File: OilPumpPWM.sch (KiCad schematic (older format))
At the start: 3 parts, among them Q1 MMBT3904

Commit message: Checkpoint before trying 4 layer
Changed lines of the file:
@@
 $Descr A4 11693 8268
 encoding utf-8
-Sheet 26 50
+Sheet 36 37
 Title ""
 Date ""
@@
 AR Path="/60483BB8/6056205F/60583721" Ref="Q4"  Part="1"
 AR Path="/614844F4/60583721" Ref="Q1"  Part="1"
-F 0 "Q4" H 5591 3846 50  0000 L CNN
+AR Path="/622024A9/60583721" Ref="Q4"  Part="1"
+AR Path="/622119D7/60583721" Ref="Q7"  Part="1"
+F 0 "Q7" H 5591 3846 50  0000 L CNN
 F 1 "MMBT3904" H 5591 3755 50  0000 L CNN
 F 2 "Package_TO_SOT_SMD:SOT-23" H 5600 3725 50  0001 L CIN
@@
 AR Path="/60483BB8/6056205F/60583722" Ref="R1"  Part="1"
 AR Path="/614844F4/60583722" Ref="R35"  Part="1"
-F 0 "R1" V 4195 3800 50  0000 C CNN
+AR Path="/622024A9/60583722" Ref="R1"  Part="1"
+AR Path="/622119D7/60583722" Ref="R4"  Part="1"
+F 0 "R4" V 4195 3800 50  0000 C CNN
 F 1 "1K" V 4286 3800 50  0000 C CNN
 F 2 "Resistor_SMD:R_0805_2012Metric" V 4440 3790 50  0001 C CNN
@@
 AR Path="/60483BB8/6056205F/60583723" Ref="R2"  Part="1"
 AR Path="/614844F4/60583723" Ref="R36"  Part="1"
-F 0 "R2" H 7268 3246 50  0000 L CNN
+AR Path="/622024A9/60583723" Ref="R2"  Part="1"
+AR Path="/622119D7/60583723" Ref="R11"  Part="1"
+F 0 "R11" H 7268 3246 50  0000 L CNN
 F 1 "1K" H 7268 3155 50  0000 L CNN
 F 2 "Resistor_SMD:R_0805_2012Metric" V 7240 3190 50  0001 C CNN

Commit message: Routed PCB
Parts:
- Q1: JLCPCB_PN (none) -> C20526
- R35, R36: JLCPCB_PN (none) -> C17513
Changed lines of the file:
@@
 F 2 "Package_TO_SOT_SMD:SOT-23" H 5600 3725 50  0001 L CIN
 F 3 "https://www.fairchildsemi.com/datasheets/2N/2N3904.pdf" H 5400 3800 50  0001 L CNN
+F 4 "C20526" H 5400 3800 50  0001 C CNN "JLCPCB_PN"
 	1    5400 3800
 	1    0    0    -1
@@
 F 2 "Resistor_SMD:R_0805_2012Metric" V 4440 3790 50  0001 C CNN
 F 3 "~" H 4400 3800 50  0001 C CNN
+F 4 "C17513" H 4400 3800 50  0001 C CNN "JLCPCB_PN"
 	1    4400 3800
 	0    1    1    0
@@
 F 2 "Resistor_SMD:R_0805_2012Metric" V 7240 3190 50  0001 C CNN
 F 3 "~" H 7200 3200 50  0001 C CNN
+F 4 "C17513" H 7200 3200 50  0001 C CNN "JLCPCB_PN"
 	1    7200 3200
 	1    0    0    -1

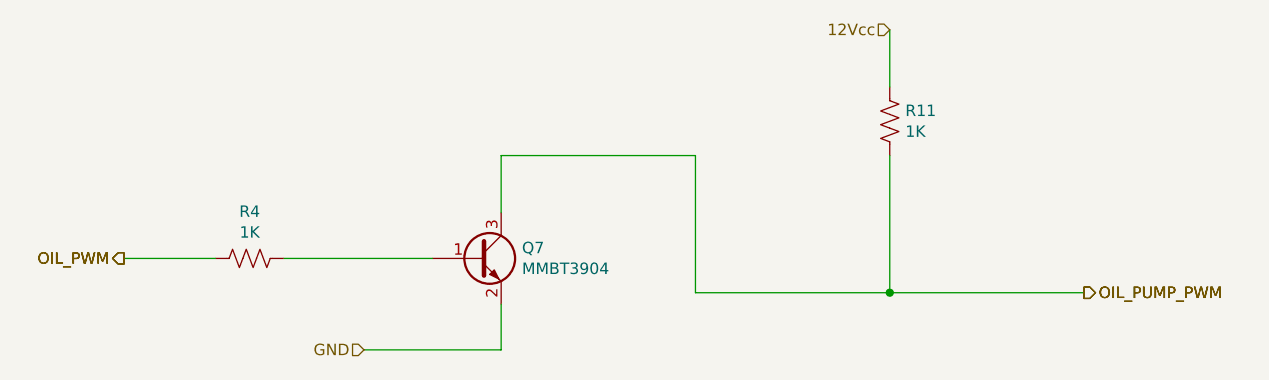
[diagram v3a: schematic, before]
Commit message: Checkpoint 2022-01-19
Design with bluepill to run the heater since we lose some of the SPI
pins to the USB port on the STM32-H107.
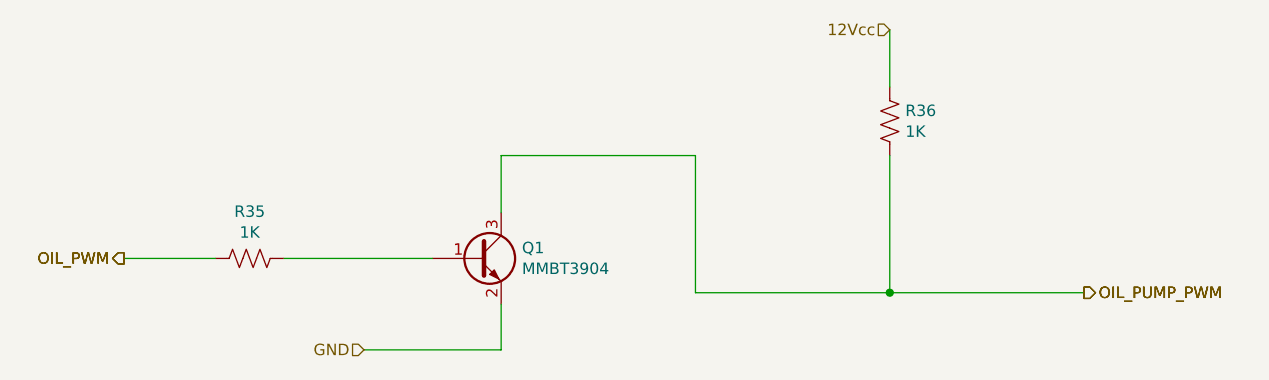
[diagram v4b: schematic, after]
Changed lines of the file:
@@
 $Descr A4 11693 8268
 encoding utf-8
-Sheet 30 36
+Sheet 29 37
 Title ""
 Date ""
@@
 AR Path="/622024A9/60583721" Ref="Q4"  Part="1"
 AR Path="/622119D7/60583721" Ref="Q7"  Part="1"
-F 0 "Q7" H 5591 3846 50  0000 L CNN
+F 0 "Q1" H 5591 3846 50  0000 L CNN
 F 1 "MMBT3904" H 5591 3755 50  0000 L CNN
 F 2 "Package_TO_SOT_SMD:SOT-23" H 5600 3725 50  0001 L CIN
@@
 AR Path="/622024A9/60583722" Ref="R1"  Part="1"
 AR Path="/622119D7/60583722" Ref="R4"  Part="1"
-F 0 "R4" V 4195 3800 50  0000 C CNN
+F 0 "R35" V 4195 3800 50  0000 C CNN
 F 1 "1K" V 4286 3800 50  0000 C CNN
 F 2 "Resistor_SMD:R_0805_2012Metric" V 4440 3790 50  0001 C CNN
@@
 AR Path="/622024A9/60583723" Ref="R2"  Part="1"
 AR Path="/622119D7/60583723" Ref="R11"  Part="1"
-F 0 "R11" H 7268 3246 50  0000 L CNN
+F 0 "R36" H 7268 3246 50  0000 L CNN
 F 1 "1K" H 7268 3155 50  0000 L CNN
 F 2 "Resistor_SMD:R_0805_2012Metric" V 7240 3190 50  0001 C CNN
